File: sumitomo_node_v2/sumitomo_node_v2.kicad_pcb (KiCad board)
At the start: 2 copper layers, 72.4 x 121.9 mm, 15 parts, among them SW1 SW_DIP_x10, U1 Arduino_Mega_2560_Without_Bot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, U2 PN532_SPI_Uart_Breakout_Board, U3 HC12

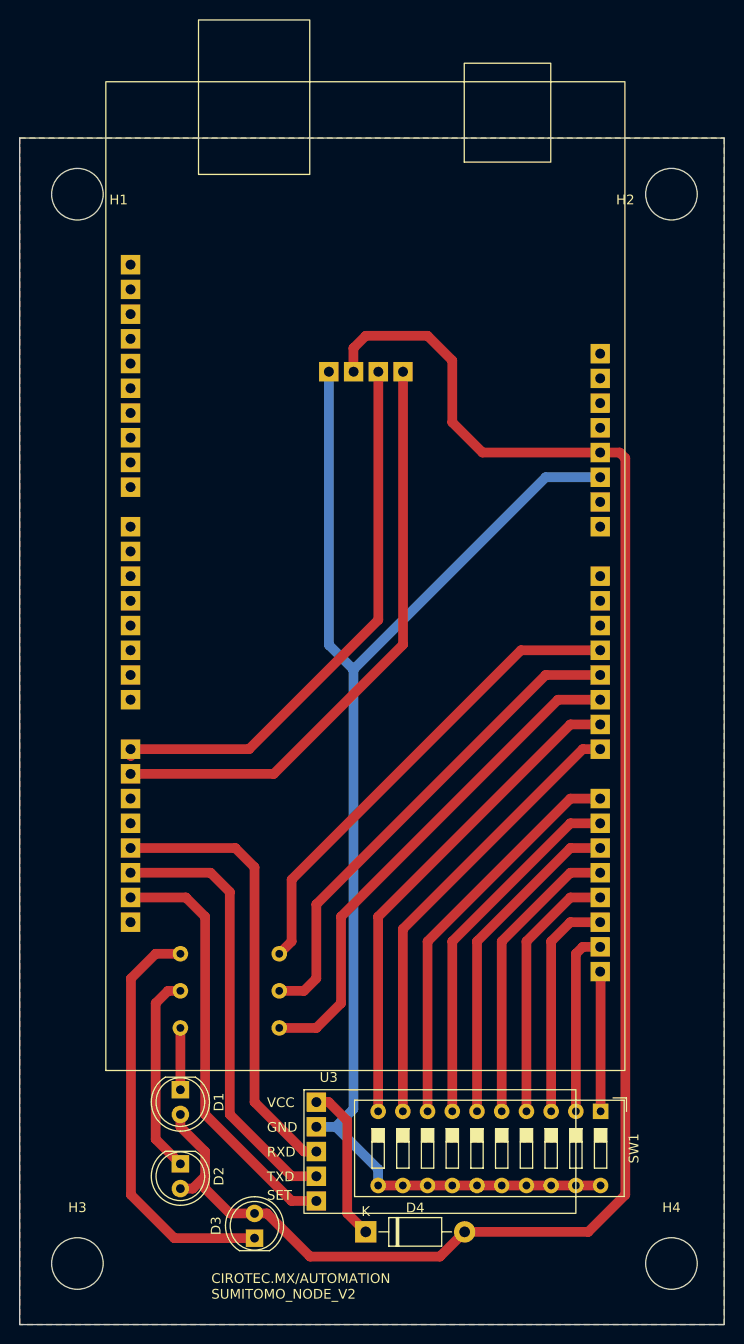
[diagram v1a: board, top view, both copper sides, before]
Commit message: Fix PN532 UART and re-route to Serial2.
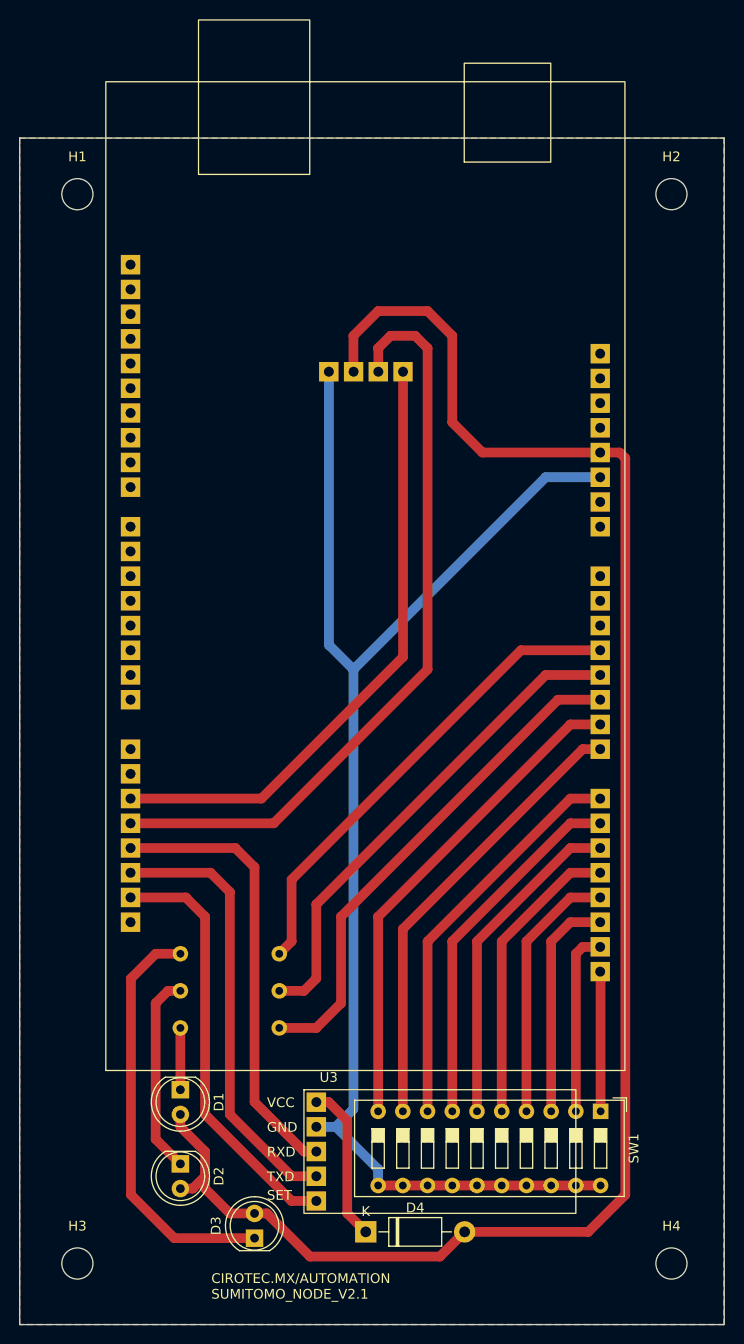
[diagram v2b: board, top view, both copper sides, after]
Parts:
- H1, H2, H3, H4: footprint MountingHole:MountingHole_5.3mm_M5_ISO7380 -> MountingHole:MountingHole_3.2mm_M3_ISO7380
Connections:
- U1 pad 43: /pn532_rx -> unconnected-(U1-D14/TX3-Pad43)
- U1 pad 44: /pn532_tx -> unconnected-(U1-D15/RX3-Pad44)
- U1 pad 45: unconnected-(U1-D16/TX2-Pad45) -> /pn532_rx
- U1 pad 46: unconnected-(U1-D17/RX2-Pad46) -> /pn532_tx
- U2 pad 3: /pn532_rx -> /pn532_tx
- U2 pad 4: /pn532_tx -> /pn532_rx
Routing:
- net /pn532_tx: track 61.5 -> 78.6 mm
- net /pn532_rx: track 57.2 -> 63.3 mm
- net +5V: track 176.2 -> 180.5 mm
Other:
- board text added: "CIROTEC.MX/AUTOMATION SUMITOMO_NODE_V2.1"
- board text removed: "CIROTEC.MX/AUTOMATION SUMITOMO_NODE_V2"
